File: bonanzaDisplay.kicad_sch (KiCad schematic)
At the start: 64 parts, among them J1 OLED-1.31-SSD1322, J15 SWD, J5 Conn_01x10, J6 USB_C_Receptacle_USB2.0, SW1 TS-1088-AR02016, SW2 TS-1088-AR02016, SW4 7*7*5-6P WX, U1 RP2354A, U10 TPS82130, U2 XC6206, U3 XC6206, Y1 ABM8-272-T3

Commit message: added missing 3d CAD. finished routing
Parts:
- removed C37: 1uF, Capacitor_SMD:C_0402_1005Metric, symbol Device:C_Small
- U1: footprint Package_DFN_QFN:QFN-60-1EP_7x7mm_P0.4mm_EP3.4x3.4mm -> bonanzaDisplay:QFN-60-1EP_7x7mm_P0.4mm_EP3.4x3.4mm
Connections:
- net CS: now also U1.15 (GPIO11); no longer U1.16 (GPIO12)
- net D0: now also U1.10 (GPIO7); no longer U1.2 (GPIO0)
- net D1: now also U1.9 (GPIO6); no longer U1.3 (GPIO1)
- net D2: now also U1.8 (GPIO5); no longer U1.4 (GPIO2)
- net D3: now also U1.7 (GPIO4); no longer U1.5 (GPIO3)
- net D4: now also U1.5 (GPIO3); no longer U1.7 (GPIO4)
- net D5: now also U1.4 (GPIO2); no longer U1.8 (GPIO5)
- net D6: now also U1.3 (GPIO1); no longer U1.9 (GPIO6)
- net D7: now also U1.2 (GPIO0); no longer U1.10 (GPIO7)
- net GND: now also C38.2, C39.2, C40.2, U2.1 (GND), U3.1 (GND)
- net RES: now also U1.16 (GPIO12); no longer U1.15 (GPIO11)
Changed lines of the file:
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@@
 	)
 	(junction
-		(at 252.73 227.33)
-		(diameter 0)
-		(color 0 0 0 0)
-	)
-	(junction
 		(at 307.34 86.36)
 		(diameter 0)
@@
 	(wire
 		(pts
-			(xy 245.11 106.68) (xy 233.68 106.68)
+			(xy 245.11 99.06) (xy 233.68 99.06)
 		)
 		(stroke
@@
 	(wire
 		(pts
-			(xy 245.11 104.14) (xy 233.68 104.14)
+			(xy 245.11 101.6) (xy 233.68 101.6)
 		)
 		(stroke
@@
 	(wire
 		(pts
-			(xy 236.22 215.9) (xy 236.22 218.44)
-		)
-		(stroke
-			(width 0)
-			(type default)
-		)
-	)
-	(wire
-		(pts
 			(xy 163.83 58.42) (xy 163.83 60.96)
 		)
@@
 	(wire
 		(pts
-			(xy 245.11 101.6) (xy 233.68 101.6)
+			(xy 245.11 104.14) (xy 233.68 104.14)
 		)
 		(stroke
@@
 	(wire
 		(pts
-			(xy 245.11 93.98) (xy 233.68 93.98)
+			(xy 245.11 111.76) (xy 233.68 111.76)
 		)
 		(stroke
@@
 	(wire
 		(pts
-			(xy 236.22 227.33) (xy 252.73 227.33)
-		)
-		(stroke
-			(width 0)
-			(type default)
-		)
-	)
-	(wire
-		(pts
 			(xy 71.12 81.28) (xy 57.15 81.28)
 		)
@@
 	(wire
 		(pts
-			(xy 245.11 99.06) (xy 233.68 99.06)
+			(xy 245.11 106.68) (xy 233.68 106.68)
 		)
 		(stroke
@@
 	(wire
 		(pts
-			(xy 236.22 223.52) (xy 236.22 227.33)
-		)
-		(stroke
-			(width 0)
-			(type default)
-		)
-	)
-	(wire
-		(pts
 			(xy 247.65 149.86) (xy 233.68 149.86)
 		)
@@
 	(wire
 		(pts
-			(xy 245.11 124.46) (xy 233.68 124.46)
+			(xy 245.11 121.92) (xy 233.68 121.92)
 		)
 		(stroke
@@
 	(wire
 		(pts
-			(xy 245.11 109.22) (xy 233.68 109.22)
+			(xy 245.11 96.52) (xy 233.68 96.52)
 		)
 		(stroke
@@
 	(wire
 		(pts
-			(xy 245.11 96.52) (xy 233.68 96.52)
+			(xy 245.11 109.22) (xy 233.68 109.22)
 		)
 		(stroke
@@
 	(wire
 		(pts
-			(xy 245.11 121.92) (xy 233.68 121.92)
+			(xy 245.11 124.46) (xy 233.68 124.46)
 		)
 		(stroke
@@
 	(wire
 		(pts
-			(xy 245.11 111.76) (xy 233.68 111.76)
+			(xy 245.11 93.98) (xy 233.68 93.98)
 		)
 		(stroke
@@
 	)
 	(label "D4"
-		(at 245.11 104.14 180)
+		(at 245.11 101.6 180)
 		(effects
 			(font
@@
 		)
 	)
+	(label "GND"
+		(at 256.54 227.33 0)
+		(effects
+			(font
+				(size 1.27 1.27)
+			)
+			(justify left bottom)
+		)
+	)
 	(label "12V"
 		(at 326.39 208.28 0)
@@
 	)
 	(label "D3"
-		(at 245.11 101.6 180)
+		(at 245.11 104.14 180)
 		(effects
 			(font
@@
 	)
 	(label "D0"
-		(at 245.11 93.98 180)
+		(at 245.11 111.76 180)
 		(effects
 			(font
@@
 	)
 	(label "D1"
-		(at 245.11 96.52 180)
+		(at 245.11 109.22 180)
 		(effects
 			(font
@@
 	)
 	(label "D7"
-		(at 245.11 111.76 180)
+		(at 245.11 93.98 180)
 		(effects
 			(font
@@
 	)
 	(label "RES"
-		(at 245.11 121.92 180)
+		(at 245.11 124.46 180)
 		(effects
 			(font
@@
 	)
 	(label "D6"
-		(at 245.11 109.22 180)
+		(at 245.11 96.52 180)
 		(effects
 			(font
@@
 	)
 	(label "D2"
-		(at 245.11 99.06 180)
+		(at 245.11 106.68 180)
 		(effects
 			(font
@@
 		)
 	)
+	(label "GND"
+		(at 256.54 251.46 0)
+		(effects
+			(font
+				(size 1.27 1.27)
+			)
+			(justify left bottom)
+		)
+	)
 	(label "DISP_SDA"
 		(at 71.12 101.6 180)
@@
 	)
 	(label "D5"
-		(at 245.11 106.68 180)
+		(at 245.11 99.06 180)
 		(effects
 			(font
@@
 	)
 	(label "CS"
-		(at 245.11 124.46 180)
+		(at 245.11 121.92 180)
 		(effects
 			(font
@@
 			)
 		)
-		(property "Footprint" "Package_DFN_QFN:QFN-60-1EP_7x7mm_P0.4mm_EP3.4x3.4mm"
+		(property "Footprint" "bonanzaDisplay:QFN-60-1EP_7x7mm_P0.4mm_EP3.4x3.4mm"
 			(at 203.2 127 0)
 			(hide yes)
@@
 					(unit 1)
 				)
-			)
-		)
-	)
-	(symbol
-		(lib_id "Device:C_Small")
-		(at 236.22 220.98 0)
-		(unit 1)
-		(body_style 1)
-		(exclude_from_sim no)
-		(in_bom yes)
-		(on_board yes)
-		(in_pos_files yes)
-		(dnp no)
-		(property "Reference" "C37"
-			(at 236.728 218.948 0)
-			(show_name no)
-			(do_not_autoplace no)
-			(effects
-				(font
-					(size 1.27 1.27)
-				)
-				(justify left)
-			)
-		)
-		(property "Value" "1uF"
-			(at 236.728 223.012 0)
-			(show_name no)
-			(do_not_autoplace no)
-			(effects
-				(font
-					(size 1.27 1.27)
-				)
-				(justify left)
-			)
-		)
-		(property "Footprint" "Capacitor_SMD:C_0402_1005Metric"
-			(at 236.22 220.98 0)
-			(hide yes)
-			(show_name no)
-			(do_not_autoplace no)
-			(effects
-				(font
-					(size 1.27 1.27)
-				)
-			)
-		)
-		(property "Datasheet" ""
-			(at 236.22 220.98 0)
-			(hide yes)
-			(show_name no)
-			(do_not_autoplace no)
-			(effects
-				(font
-					(size 1.27 1.27)
-				)
-			)
-		)
-		(property "Description" "Unpolarized capacitor, small symbol"
-			(at 236.22 220.98 0)
-			(hide yes)
-			(show_name no)
-			(do_not_autoplace no)
-			(effects
-				(font
-					(size 1.27 1.27)
-				)
-			)
-		)
-		(property "Digi-Key Part Number" ""
-			(at 236.22 220.98 0)
-			(hide yes)
-			(show_name no)
-			(do_not_autoplace no)
-			(effects
-				(font
-					(size 1.27 1.27)
-				)
-			)
-		)
-		(property "MPN" ""
-			(at 236.22 220.98 0)
-			(hide yes)
-			(show_name no)
-			(do_not_autoplace no)
-			(effects
-				(font
-					(size 1.27 1.27)
-				)
-			)
-		)
-		(property "Manufacturer" ""
-			(at 236.22 220.98 0)
-			(hide yes)
-			(show_name no)
-			(do_not_autoplace no)
-			(effects
-				(font
-					(size 1.27 1.27)
-				)
-			)
-		)
-		(property "Supplier" ""
-			(at 236.22 220.98 0)
-			(hide yes)
-			(show_name no)
-			(do_not_autoplace no)
-			(effects
-				(font
-					(size 1.27 1.27)
-				)
-			)
-		)
-		(pin "1"
-		)
-		(pin "2"
-		)
-		(instances
-			(project "bonanzaDisplay"
-				(path "/7e582155-2c81-495e-af6e-58d19d09acab"
-					(reference "C37")
-					(unit 1)
-				)

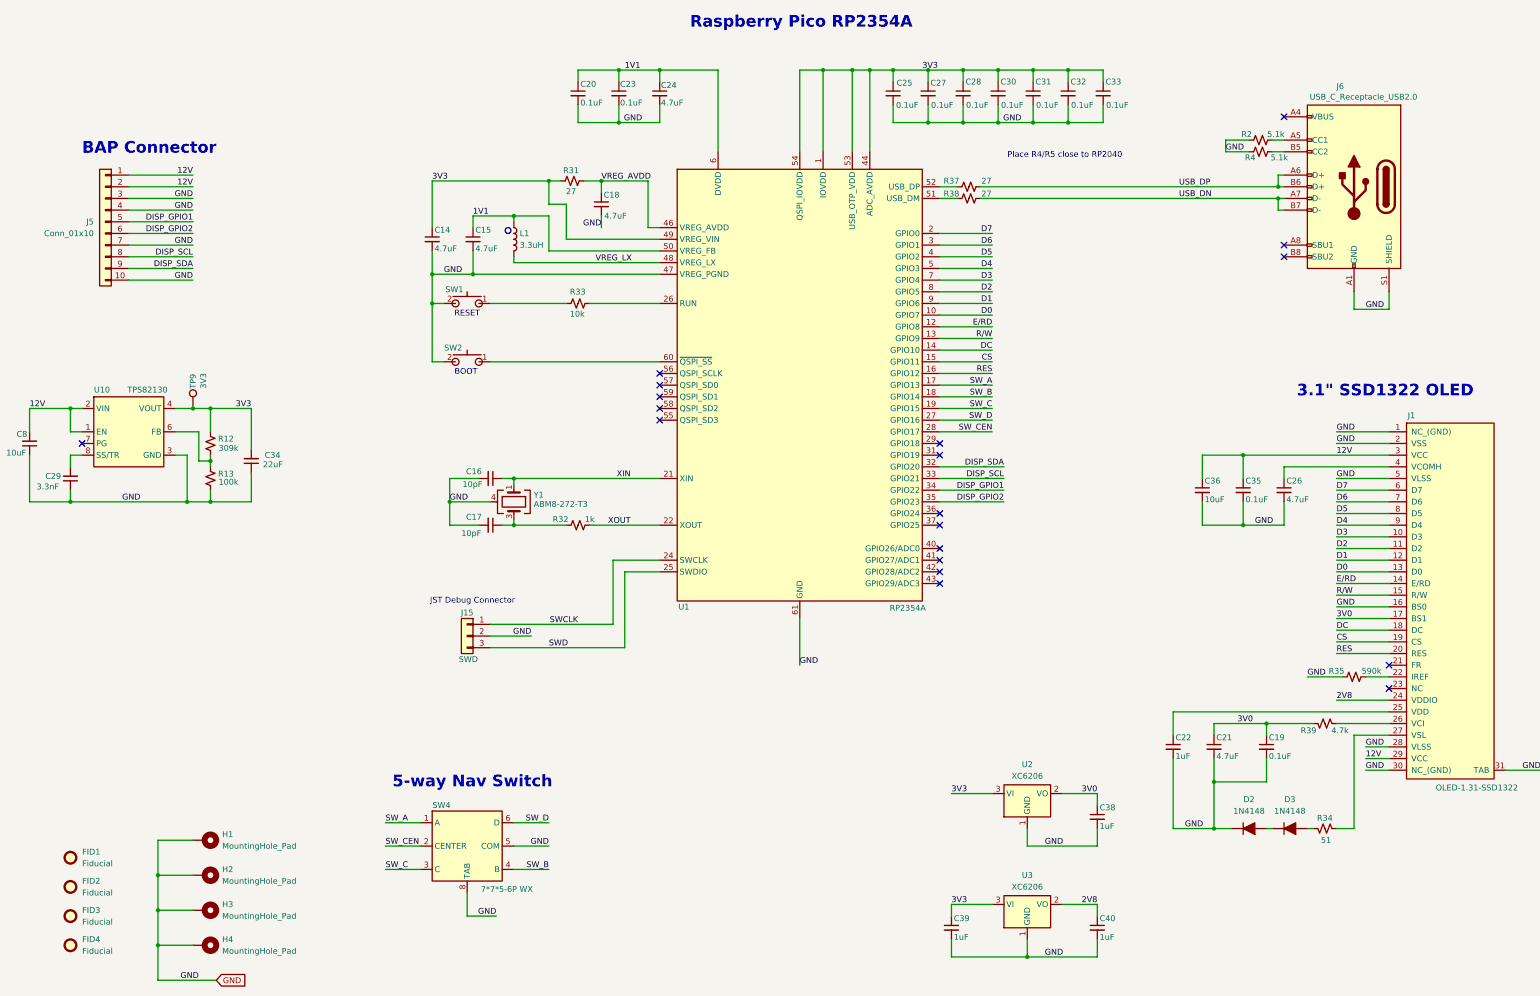
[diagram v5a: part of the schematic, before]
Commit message: routing cleanup
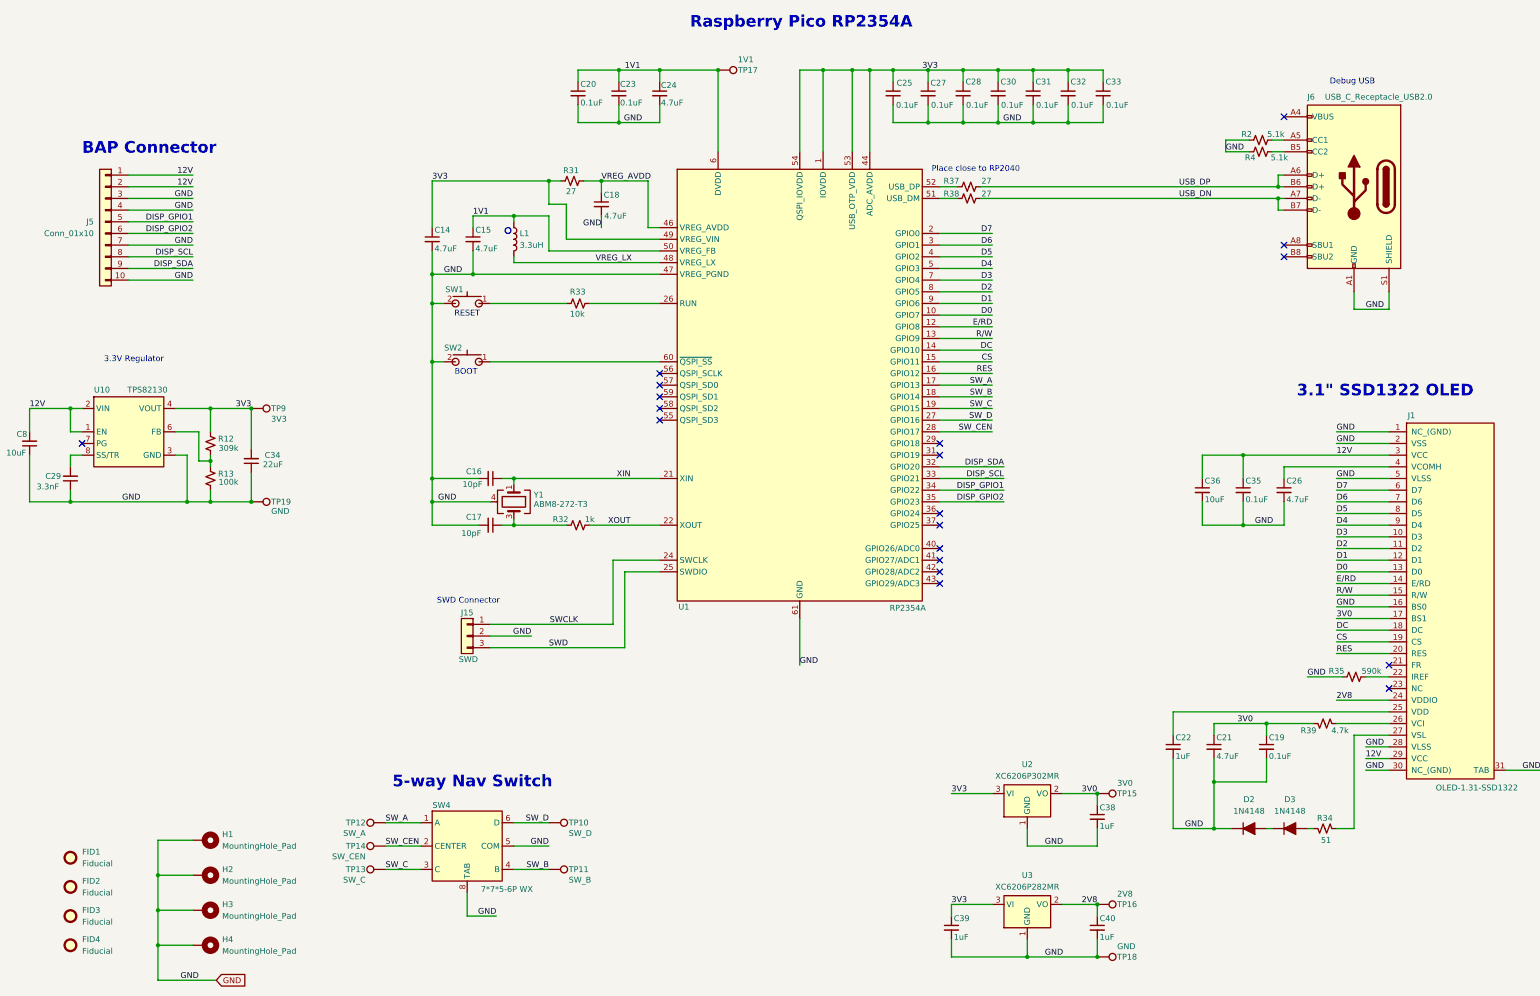
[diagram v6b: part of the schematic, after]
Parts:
- added TP10: SW_D, bonanzaDisplay:TestPoint_Pad_D1.0mm, symbol Connector:TestPoint
- added TP11: SW_B, bonanzaDisplay:TestPoint_Pad_D1.0mm, symbol Connector:TestPoint
- added TP12: SW_A, bonanzaDisplay:TestPoint_Pad_D1.0mm, symbol Connector:TestPoint
- added TP13: SW_C, bonanzaDisplay:TestPoint_Pad_D1.0mm, symbol Connector:TestPoint
- added TP14: SW_CEN, bonanzaDisplay:TestPoint_Pad_D1.0mm, symbol Connector:TestPoint
- added TP15: 3V0, bonanzaDisplay:TestPoint_Pad_D1.0mm, symbol Connector:TestPoint
- added TP16: 2V8, bonanzaDisplay:TestPoint_Pad_D1.0mm, symbol Connector:TestPoint
- added TP17: 1V1, bonanzaDisplay:TestPoint_Pad_D1.0mm, symbol Connector:TestPoint
- added TP18, TP19: GND, bonanzaDisplay:TestPoint_Pad_D1.0mm, symbol Connector:TestPoint
- J15: now left out of the parts list
- U2: value XC6206 -> XC6206P302MR
- U3: value XC6206 -> XC6206P282MR
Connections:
- net 1V1: now also TP17.1
- net 2V8: now also TP16.1
- net 3V0: now also TP15.1
- net GND: now also TP18.1, TP19.1
- net SW_A: now also TP12.1
- net SW_B: now also TP11.1
- net SW_C: now also TP13.1
- net SW_CEN: now also TP14.1
- net SW_D: now also TP10.1
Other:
- note added: "3.3V Regulator"
- note added: "Debug USB"
- note added: "Place close to RP2040"
- note added: "SWD Connector"
- note removed: "JST Debug Connector"
- note removed: "Place R4/R5 close to RP2040"
- moved on the sheet: TP9

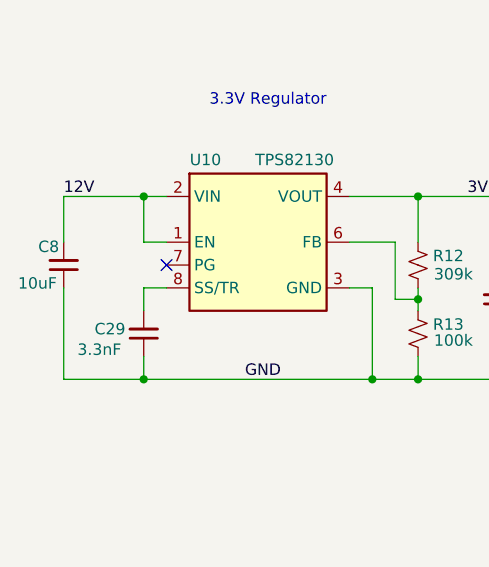
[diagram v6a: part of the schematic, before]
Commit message: updated RP2354A inductor footprint. fixed USB port position. fixed corrupted footprint library
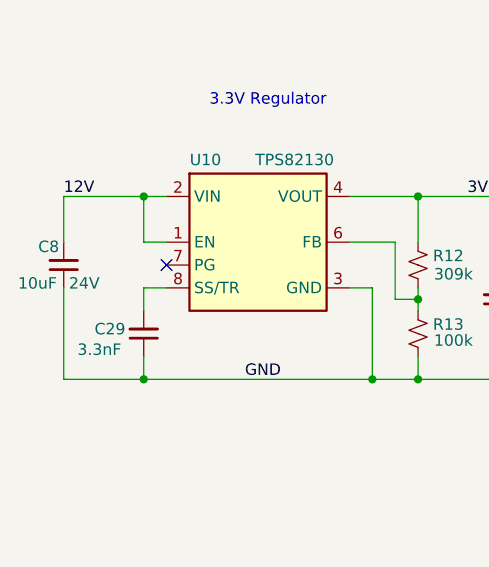
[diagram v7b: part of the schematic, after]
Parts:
- C8: Voltage (none) -> 24V
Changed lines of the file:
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@@
+			)
+		)
+		(property "Voltage" "24V"
+			(at 37.846 141.732 0)
+			(show_name no)
+			(do_not_autoplace no)
+			(effects
+				(font
+					(size 1.27 1.27)
+				)
 			)
 		)
